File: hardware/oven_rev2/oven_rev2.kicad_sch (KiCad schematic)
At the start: 22 parts, among them J1 RELAY_CTRL, J10 5V_IN, J2 SERIAL, J3 NUMPAD, J4 AVR-ISP-6, J5 LIVE, J6 DISPLAY, J7 RELAY_PWR, J8 OUTPUT, J9 NEUTRAL, U1 ATmega328-AU, U2 MAX6675, Y1 16M

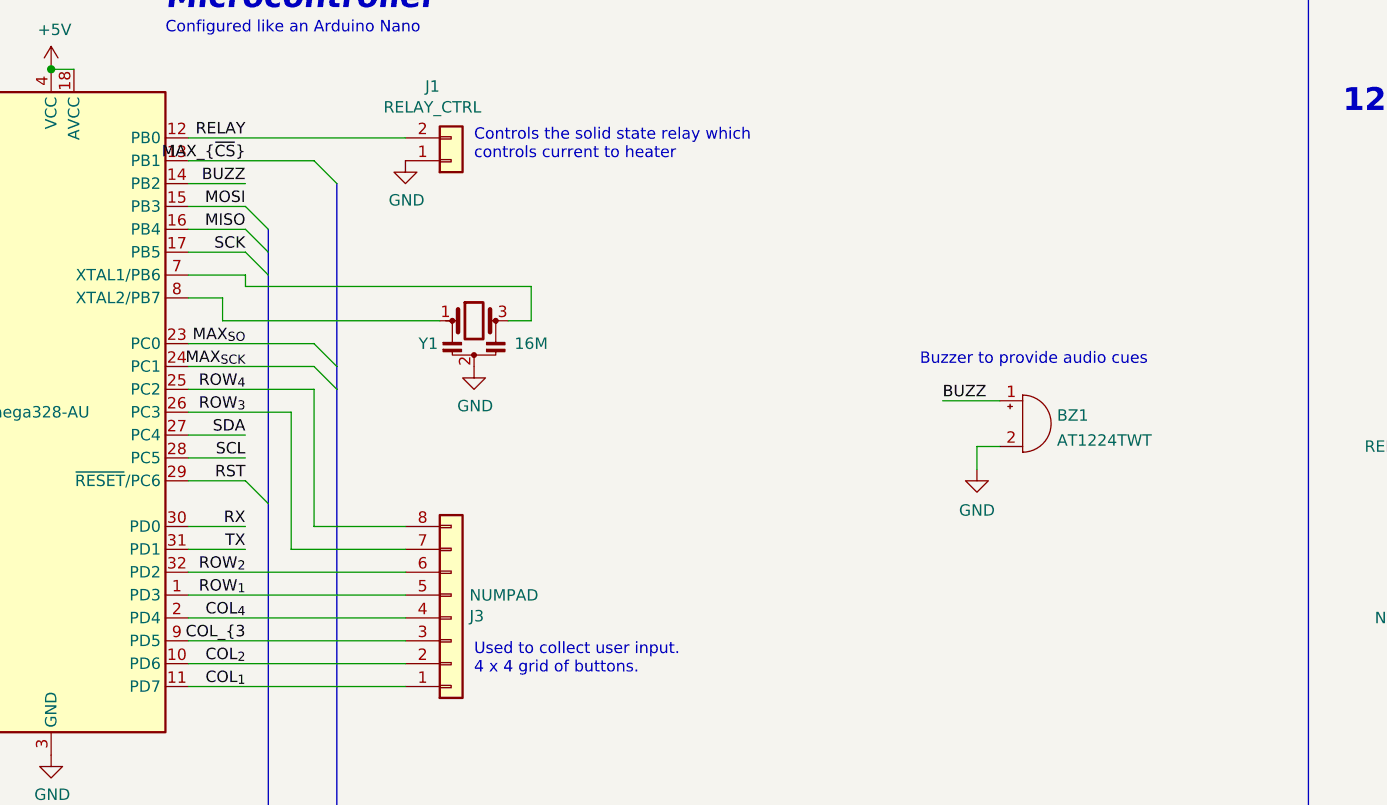
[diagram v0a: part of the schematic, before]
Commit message: Removed buzzer that was not present in fabricated boards
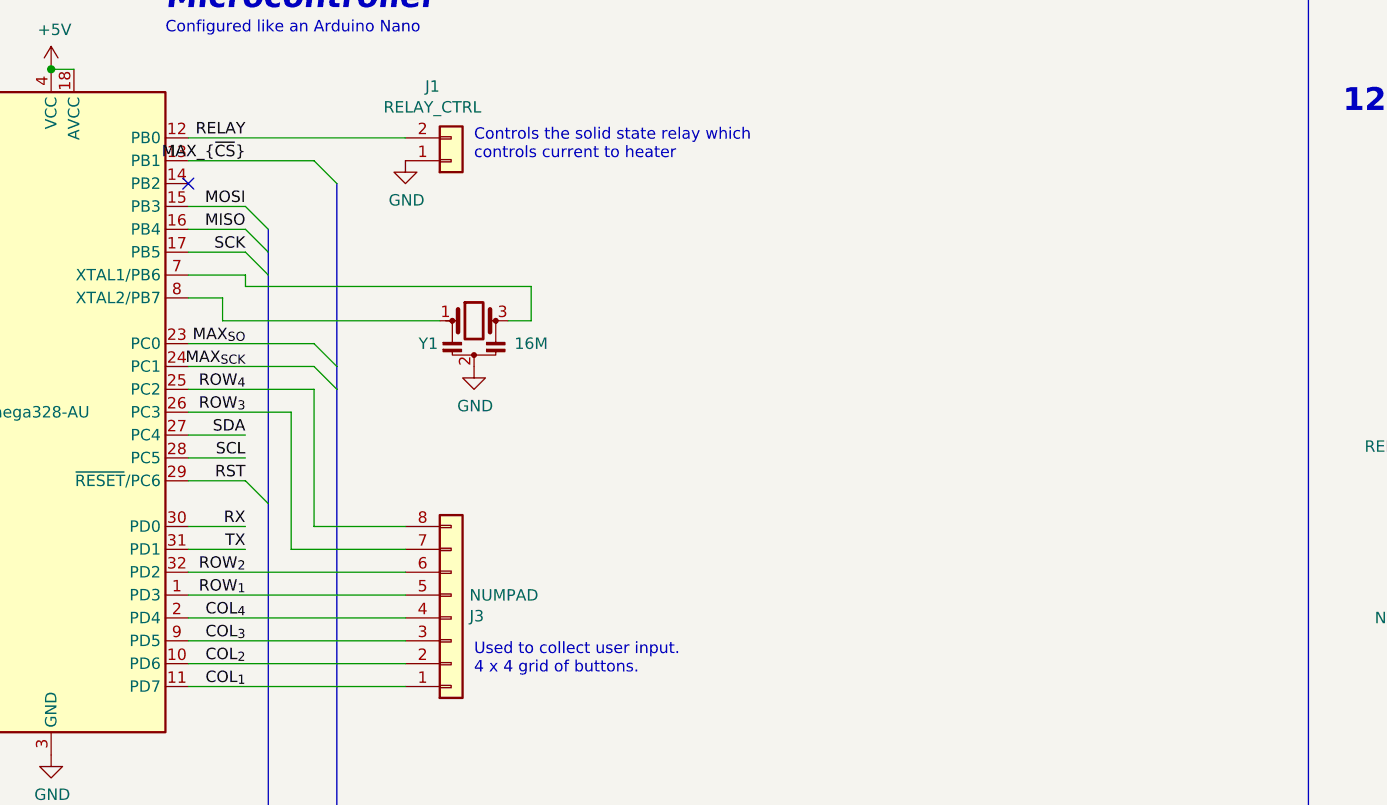
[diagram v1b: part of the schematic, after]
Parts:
- removed BZ1: AT1224TWT, Buzzer_Beeper:MagneticBuzzer_ProSignal_ABT-410-RC, symbol Device:Buzzer
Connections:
- net BUZZ: no longer names the net of U1.14 (PB2)
- net COL_{3 renamed COL_{3}
- no-connect marks 6 -> 7
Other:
- note removed: "Buzzer to provide audio cues"
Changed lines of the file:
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@@
   (no_connect (at 30.48 41.91))
   (no_connect (at 30.48 39.37))
+  (no_connect (at 60.96 39.37))
   (no_connect (at 229.87 72.39))
   (bus_entry (at 67.31 72.39) (size 2.54 2.54)
@@
     (stroke (width 0) (type default))
   )
-  (wire (pts (xy 151.13 68.58) (xy 148.59 68.58))
-    (stroke (width 0) (type default))
-  )
   (wire (pts (xy 228.6 64.77) (xy 229.87 64.77))
     (stroke (width 0) (type default))
@@
     (stroke (width 0) (type default))
   )
-  (wire (pts (xy 60.96 39.37) (xy 67.31 39.37))
-    (stroke (width 0) (type default))
-  )
   (wire (pts (xy 228.6 62.23) (xy 228.6 64.77))
-    (stroke (width 0) (type default))
-  )
-  (wire (pts (xy 144.78 63.5) (xy 151.13 63.5))
     (stroke (width 0) (type default))
   )
@@
   (polyline (pts (xy 185.42 111.76) (xy 264.16 111.76))
     (stroke (width 0.3048) (type default))
-  )
-  (wire (pts (xy 148.59 68.58) (xy 148.59 71.12))
-    (stroke (width 0) (type default))
   )
   (wire (pts (xy 67.31 77.47) (xy 60.96 77.47))
@@
     (effects (font (size 2.54 2.54) (thickness 0.508) bold italic) (justify left bottom))
   )
-  (text "Buzzer to provide audio cues" (at 142.24 59.69 0)
-    (effects (font (size 1.27 1.27)) (justify left bottom))
-  )
   (text "Display Connection" (at 119.38 124.46 0)
     (effects (font (size 2.54 2.54) (thickness 0.508) bold italic) (justify left bottom))
@@
     (effects (font (size 1.27 1.27)) (justify right bottom))
   )
-  (label "COL_{3" (at 67.31 90.17 180) (fields_autoplaced)
+  (label "COL_{3}" (at 67.31 90.17 180) (fields_autoplaced)
     (effects (font (size 1.27 1.27)) (justify right bottom))
   )
@@
     (effects (font (size 1.27 1.27)) (justify right bottom))
   )
-  (label "BUZZ" (at 144.78 63.5 0) (fields_autoplaced)
-    (effects (font (size 1.27 1.27)) (justify left bottom))
-  )
   (label "MAX_{~{CS}}" (at 67.31 36.83 180) (fields_autoplaced)
-    (effects (font (size 1.27 1.27)) (justify right bottom))
-  )
-  (label "BUZZ" (at 67.31 39.37 180) (fields_autoplaced)
     (effects (font (size 1.27 1.27)) (justify right bottom))
   )
@@
         )
       )
-    )
-  )
-  (symbol (lib_id "power:GND") (at 148.59 71.12 0) (unit 1)
-    (in_bom yes) (on_board yes) (dnp no) (fields_autoplaced)
-    (property "Reference" "#PWR05" (at 148.59 77.47 0)
-      (effects (font (size 1.27 1.27)) hide)
-    )
-    (property "Value" "GND" (at 148.59 75.6825 0)
-      (effects (font (size 1.27 1.27)))
-    )
-    (property "Footprint" "" (at 148.59 71.12 0)
-      (effects (font (size 1.27 1.27)) hide)
-    )
-    (property "Datasheet" "" (at 148.59 71.12 0)
-      (effects (font (size 1.27 1.27)) hide)
-    )
-    (pin "1")
-    (instances
-      (project "oven_rev2"
-        (path "/581ddb5d-4155-448c-9162-b92ba6b86570"
-          (reference "#PWR05") (unit 1)
-        )
-      )
-    )
-  )
-  (symbol (lib_id "Device:Buzzer") (at 153.67 66.04 0) (unit 1)
-    (in_bom yes) (on_board yes) (dnp no) (fields_autoplaced)
-    (property "Reference" "BZ1" (at 157.48 65.1315 0)
-      (effects (font (size 1.27 1.27)) (justify left))
-    )
-    (property "Value" "AT1224TWT" (at 157.48 67.9066 0)
-      (effects (font (size 1.27 1.27)) (justify left))
-    )
-    (property "Footprint" "Buzzer_Beeper:MagneticBuzzer_ProSignal_ABT-410-RC" (at 153.035 63.5 90)
-      (effects (font (size 1.27 1.27)) hide)
-    )
-    (property "Datasheet" "~" (at 153.035 63.5 90)
-      (effects (font (size 1.27 1.27)) hide)
-    )
-    (pin "1")
-    (pin "2")
-    (instances
-      (project "oven_rev2"
-        (path "/581ddb5d-4155-448c-9162-b92ba6b86570"
-          (reference "BZ1") (unit 1)
-        )
-      )
